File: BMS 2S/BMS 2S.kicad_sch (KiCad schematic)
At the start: 24 parts, among them J1 Screw_Terminal_01x01, J2 Screw_Terminal_01x01, J3 Screw_Terminal_01x01, J4 Screw_Terminal_01x01, J5 Screw_Terminal_01x01, J6 Screw_Terminal_01x01, Q1 DMG2302UK-7, Q2 DMG2302UK-7, Q3 DMG2302UK-7, Q4 DMG2302UK-7, U1 S-8252AAZ-M6T1U, U2 S-8252AAZ-M6T1U

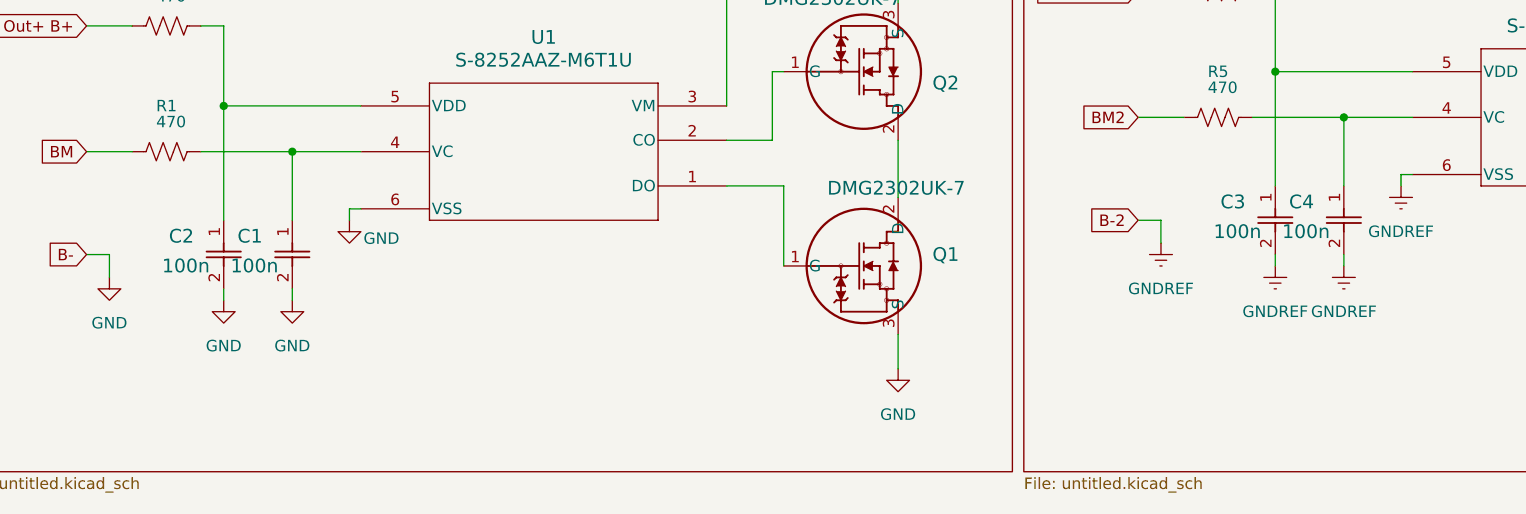
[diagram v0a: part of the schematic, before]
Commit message: BMS- Réglage des bugs de link power plane
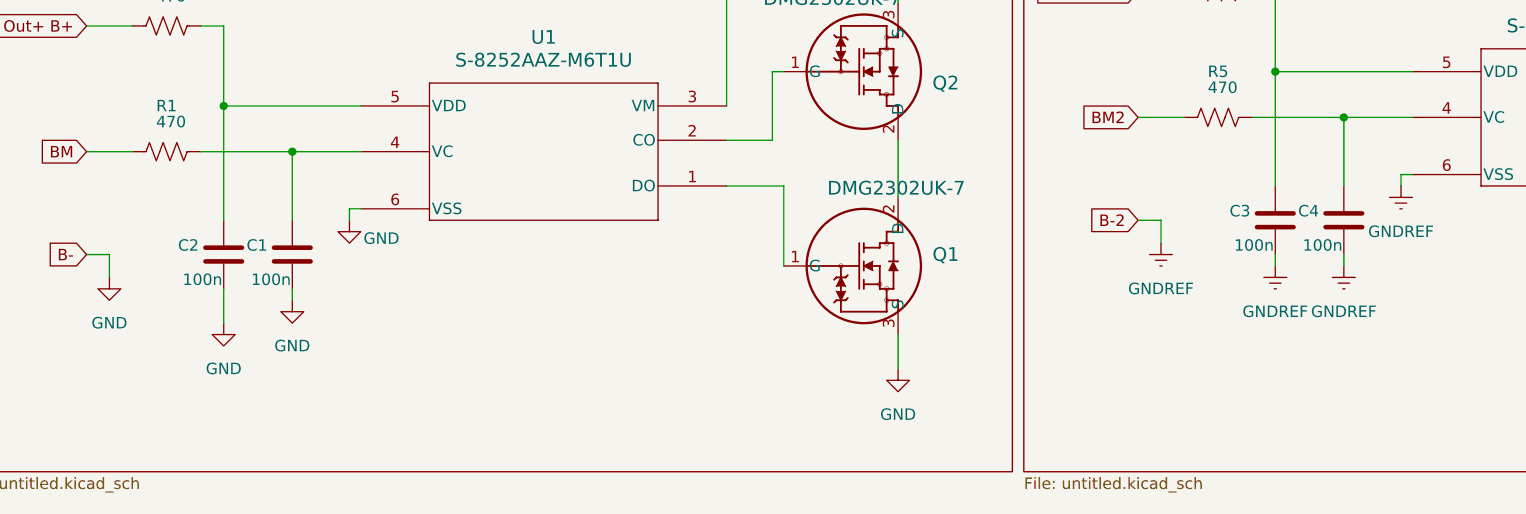
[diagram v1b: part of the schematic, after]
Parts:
- removed C1, C2, C3, C4: 100n, CAPC370195_140N_KEM, symbol BMS_schematics:C1206X104K2RACAUTO
- added C1, C2, C3, C4: 100n, C_1206_3216Metric_Pad1.33x1.80mm_HandSolder, symbol Device:C
- J1, J2, J3, J4, J5, J6: footprint (none) -> MountingHole_3.2mm_M3_DIN965_Pad
- OUT1: footprint (none) -> AMASS_XT60-M_1x02_P7.20mm_Vertical
- R1, R2, R3, R4, R5, R6: footprint (none) -> R_1206_3216Metric_Pad1.30x1.75mm_HandSolder
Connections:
- net GND: now also C1.2, C2.2
- net GNDREF: now also C3.2, C4.2
- net at R2.1, U1.5 (VDD): now also C2.1
- net at R1.1, U1.4 (VC): now also C1.1
- net at R4.1, U2.5 (VDD): now also C3.1
- net at R5.1, U2.4 (VC): now also C4.1
